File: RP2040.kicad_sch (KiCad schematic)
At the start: 16 parts, among them U1 RP2040

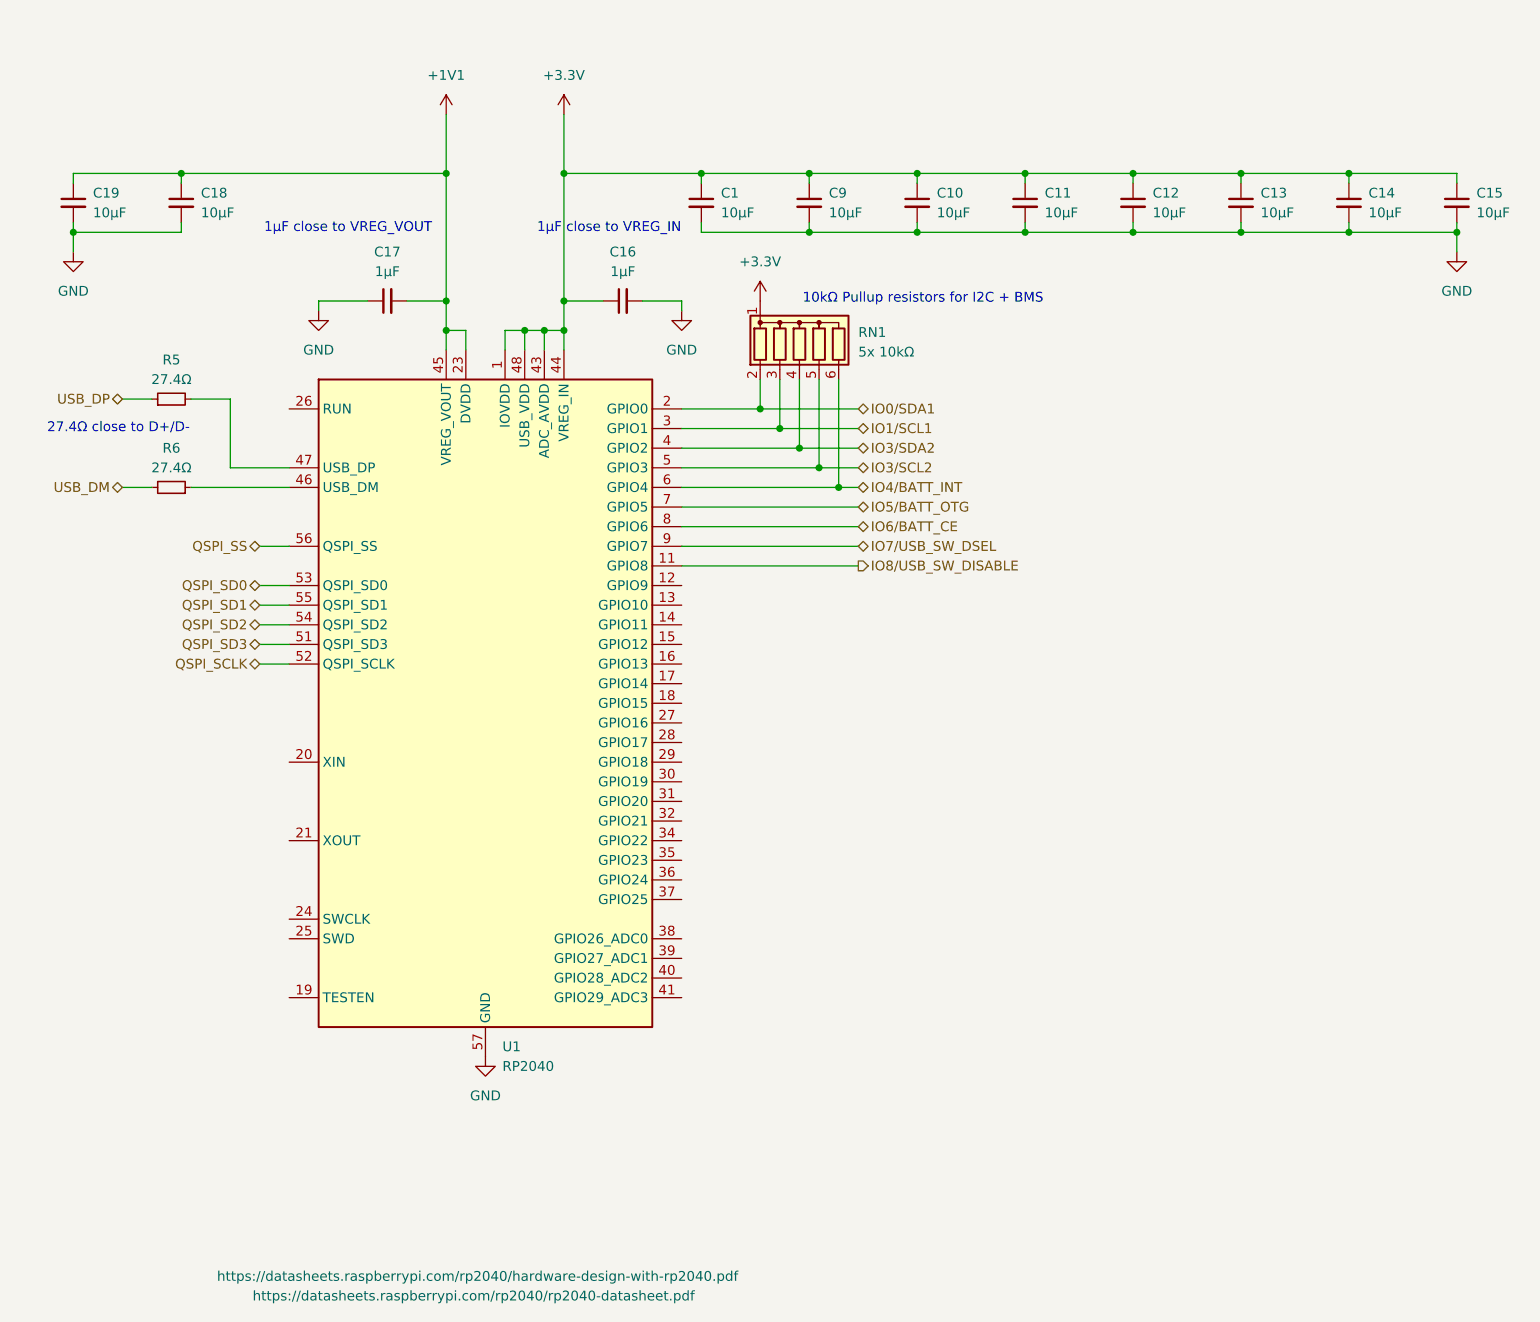
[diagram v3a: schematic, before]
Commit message: BMS updates
Added missing capacitor for OTG
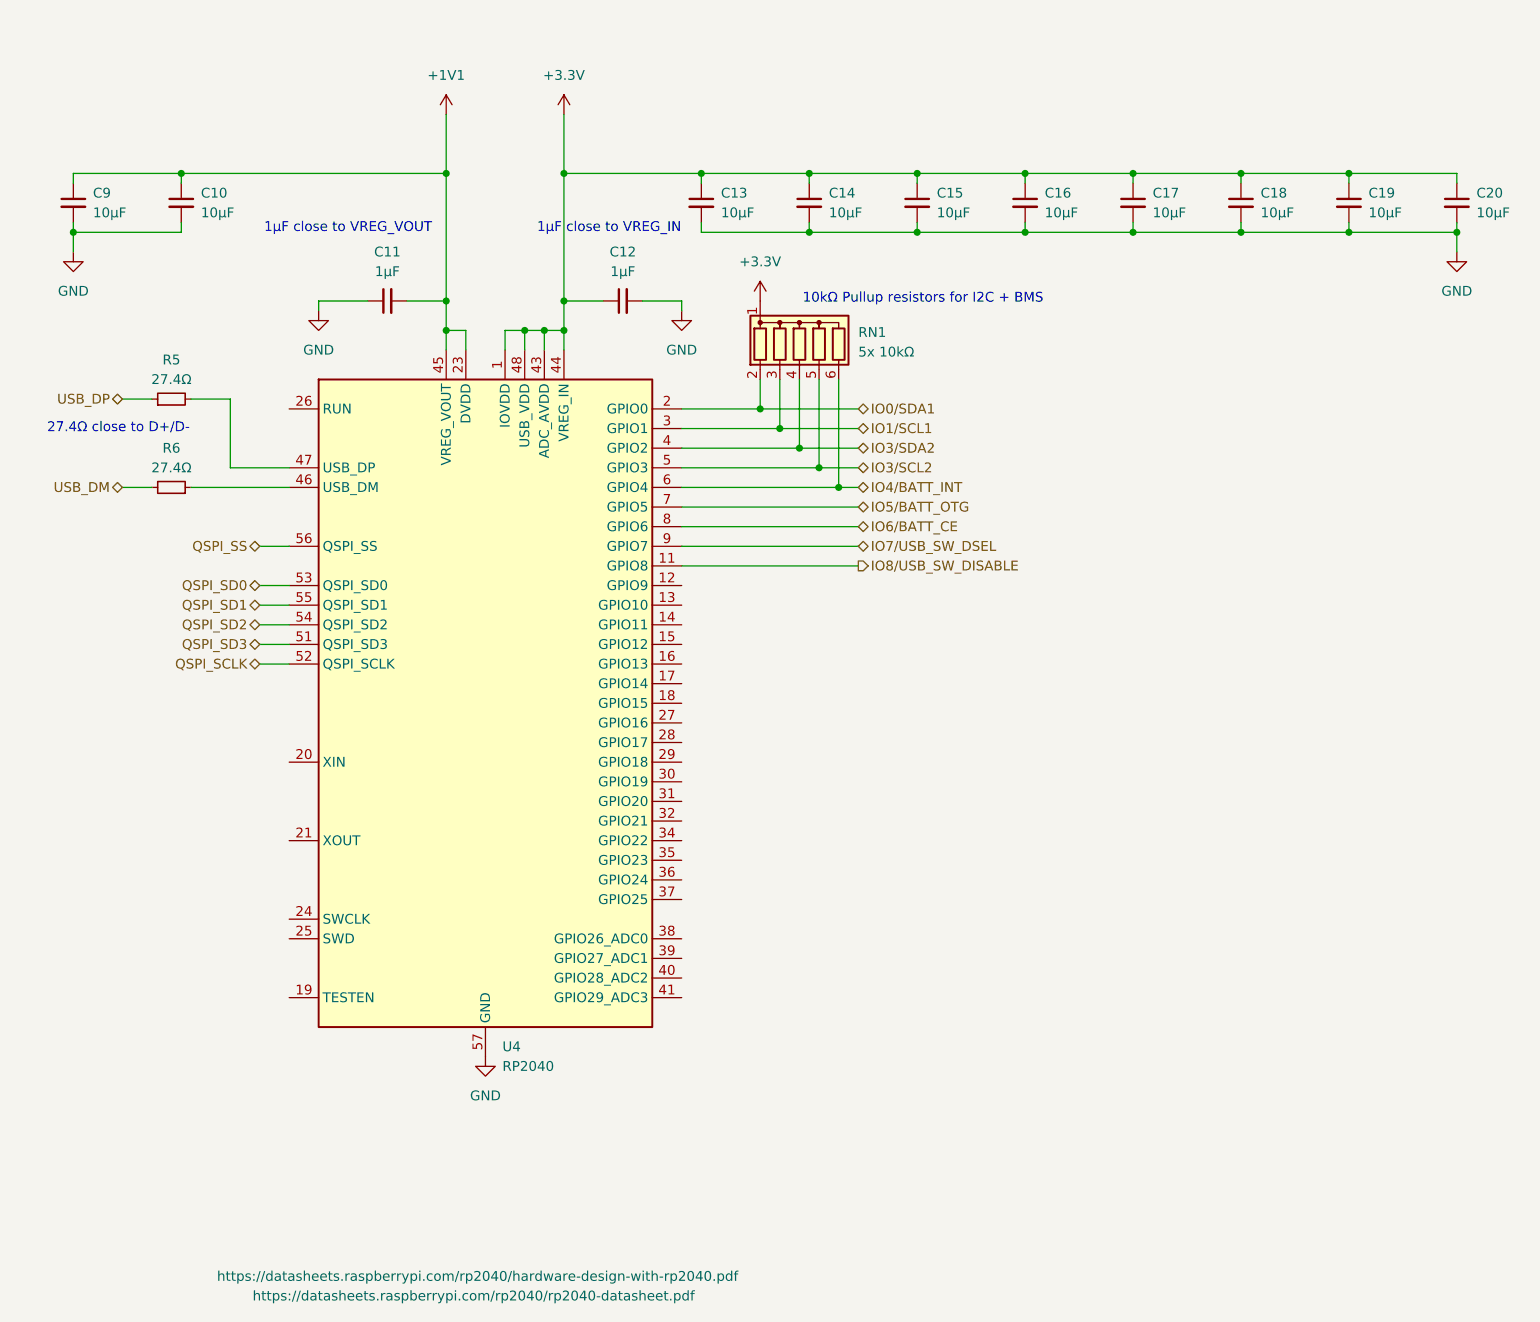
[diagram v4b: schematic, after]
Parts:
- renumbered C18 to C10, C17 to C11, C16 to C12, C1 to C13, C9 to C14, C10 to C15, C11 to C16, C12 to C17, C13 to C18, C14 to C19, C15 to C20, C19 to C9, U1 to U4
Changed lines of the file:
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@@
 		(on_board yes)
 		(dnp no)
-		(property "Reference" "C18"
+		(property "Reference" "C10"
 			(at 69.85 44.45 0)
 			(effects
@@
 			(project "Minibadge Display 5x3"
 				(path "/e5119d15-74fb-4259-abbc-5cab1f368532/9c03ac80-c552-4a59-83c4-4e8b67a63031"
-					(reference "C18")
+					(reference "C10")
 					(unit 1)
 				)
@@
 		(dnp no)
 		(fields_autoplaced yes)
-		(property "Reference" "#PWR01"
+		(property "Reference" "#PWR030"
 			(at 106.68 162.56 0)
 			(effects
@@
 			(project "Minibadge Display 5x3"
 				(path "/e5119d15-74fb-4259-abbc-5cab1f368532/9c03ac80-c552-4a59-83c4-4e8b67a63031"
-					(reference "#PWR01")
+					(reference "#PWR030")
 					(unit 1)
 				)
@@
 		(on_board yes)
 		(dnp no)
-		(property "Reference" "C9"
+		(property "Reference" "C14"
 			(at 151.13 44.45 0)
 			(effects
@@
 			(project ""
 				(path "/e5119d15-74fb-4259-abbc-5cab1f368532/9c03ac80-c552-4a59-83c4-4e8b67a63031"
-					(reference "C9")
+					(reference "C14")
 					(unit 1)
 				)
@@
 		(on_board yes)
 		(dnp no)
-		(property "Reference" "C11"
+		(property "Reference" "C16"
 			(at 179.07 44.45 0)
 			(effects
@@
 			(project "Minibadge Display 5x3"
 				(path "/e5119d15-74fb-4259-abbc-5cab1f368532/9c03ac80-c552-4a59-83c4-4e8b67a63031"
-					(reference "C11")
+					(reference "C16")
 					(unit 1)
 				)
@@
 		(dnp no)
 		(fields_autoplaced yes)
-		(property "Reference" "#PWR0117"
+		(property "Reference" "#PWR029"
 			(at 101.6 38.1 0)
 			(effects
@@
 			(project ""
 				(path "/e5119d15-74fb-4259-abbc-5cab1f368532/9c03ac80-c552-4a59-83c4-4e8b67a63031"
-					(reference "#PWR0117")
+					(reference "#PWR029")
 					(unit 1)
 				)
@@
 		(dnp no)
 		(fields_autoplaced yes)
-		(property "Reference" "#PWR0120"
+		(property "Reference" "#PWR033"
 			(at 142.24 62.23 0)
 			(effects
@@
 			(project ""
 				(path "/e5119d15-74fb-4259-abbc-5cab1f368532/9c03ac80-c552-4a59-83c4-4e8b67a63031"
-					(reference "#PWR0120")
+					(reference "#PWR033")
 					(unit 1)
 				)
@@
 		(on_board yes)
 		(dnp no)
-		(property "Reference" "U1"
+		(property "Reference" "U4"
 			(at 108.8741 154.94 0)
 			(effects
@@
 			(project "Minibadge Display 5x3"
 				(path "/e5119d15-74fb-4259-abbc-5cab1f368532/9c03ac80-c552-4a59-83c4-4e8b67a63031"
-					(reference "U1")
+					(reference "U4")
 					(unit 1)
 				)
@@
 		(on_board yes)
 		(dnp no)
-		(property "Reference" "C1"
+		(property "Reference" "C13"
 			(at 137.16 44.45 0)
 			(effects
@@
 			(project ""
 				(path "/e5119d15-74fb-4259-abbc-5cab1f368532/9c03ac80-c552-4a59-83c4-4e8b67a63031"
-					(reference "C1")
+					(reference "C13")
 					(unit 1)
 				)
@@
 		(dnp no)
 		(fields_autoplaced yes)
-		(property "Reference" "C17"
+		(property "Reference" "C11"
 			(at 93.9863 52.07 90)
 			(effects
@@
 			(project "Minibadge Display 5x3"
 				(path "/e5119d15-74fb-4259-abbc-5cab1f368532/9c03ac80-c552-4a59-83c4-4e8b67a63031"
-					(reference "C17")
+					(reference "C11")
 					(unit 1)
 				)
@@
 		(on_board yes)
 		(dnp no)
-		(property "Reference" "C10"
+		(property "Reference" "C15"
 			(at 165.1 44.45 0)
 			(effects
@@
 			(project "Minibadge Display 5x3"
 				(path "/e5119d15-74fb-4259-abbc-5cab1f368532/9c03ac80-c552-4a59-83c4-4e8b67a63031"
-					(reference "C10")
+					(reference "C15")
 					(unit 1)
 				)
@@
 		(dnp no)
 		(fields_autoplaced yes)
-		(property "Reference" "#PWR0115"
+		(property "Reference" "#PWR034"
 			(at 232.41 58.42 0)
 			(effects
@@
 			(project ""
 				(path "/e5119d15-74fb-4259-abbc-5cab1f368532/9c03ac80-c552-4a59-83c4-4e8b67a63031"
-					(reference "#PWR0115")
+					(reference "#PWR034")
 					(unit 1)
 				)
@@
 		(on_board yes)
 		(dnp no)
-		(property "Reference" "C15"
+		(property "Reference" "C20"
 			(at 234.95 44.45 0)
 			(effects
@@
 			(project "Minibadge Display 5x3"
 				(path "/e5119d15-74fb-4259-abbc-5cab1f368532/9c03ac80-c552-4a59-83c4-4e8b67a63031"
-					(reference "C15")
+					(reference "C20")
 					(unit 1)
 				)
@@
 		(dnp no)
 		(fields_autoplaced yes)
-		(property "Reference" "#PWR0118"
+		(property "Reference" "#PWR032"
 			(at 132.08 66.04 0)
 			(effects
@@
 			(project "Minibadge Display 5x3"
 				(path "/e5119d15-74fb-4259-abbc-5cab1f368532/9c03ac80-c552-4a59-83c4-4e8b67a63031"
-					(reference "#PWR0118")
+					(reference "#PWR032")
 					(unit 1)
 				)
@@
 		(on_board yes)
 		(dnp no)
-		(property "Reference" "C19"
+		(property "Reference" "C9"
 			(at 55.88 44.45 0)
 			(effects
@@
 			(project "Minibadge Display 5x3"
 				(path "/e5119d15-74fb-4259-abbc-5cab1f368532/9c03ac80-c552-4a59-83c4-4e8b67a63031"
-					(reference "C19")
+					(reference "C9")
 					(unit 1)
 				)
@@
 		(on_board yes)
 		(dnp no)
-		(property "Reference" "C14"
+		(property "Reference" "C19"
 			(at 220.98 44.45 0)
 			(effects
@@
 			(project "Minibadge Display 5x3"
 				(path "/e5119d15-74fb-4259-abbc-5cab1f368532/9c03ac80-c552-4a59-83c4-4e8b67a63031"
-					(reference "C14")
+					(reference "C19")
 					(unit 1)
 				)
@@
 		(dnp no)
 		(fields_autoplaced yes)
-		(property "Reference" "#PWR0116"
+		(property "Reference" "#PWR028"
 			(at 85.09 66.04 0)
 			(effects
@@
 			(project "Minibadge Display 5x3"
 				(path "/e5119d15-74fb-4259-abbc-5cab1f368532/9c03ac80-c552-4a59-83c4-4e8b67a63031"
-					(reference "#PWR0116")
+					(reference "#PWR028")
 					(unit 1)
 				)
@@
 		(on_board yes)
 		(dnp no)
-		(property "Reference" "C13"
+		(property "Reference" "C18"
 			(at 207.01 44.45 0)
 			(effects
@@
 			(project "Minibadge Display 5x3"
 				(path "/e5119d15-74fb-4259-abbc-5cab1f368532/9c03ac80-c552-4a59-83c4-4e8b67a63031"
-					(reference "C13")
+					(reference "C18")
 					(unit 1)
 				)
@@
 		(dnp no)
 		(fields_autoplaced yes)
-		(property "Reference" "C16"
+		(property "Reference" "C12"
 			(at 124.4663 52.07 90)
 			(effects
@@
 			(project ""
 				(path "/e5119d15-74fb-4259-abbc-5cab1f368532/9c03ac80-c552-4a59-83c4-4e8b67a63031"
-					(reference "C16")
+					(reference "C12")
 					(unit 1)
 				)
@@
 		(dnp no)
 		(fields_autoplaced yes)
-		(property "Reference" "#PWR0119"
+		(property "Reference" "#PWR027"
 			(at 53.34 58.42 0)
 			(effects
@@
 			(project ""
 				(path "/e5119d15-74fb-4259-abbc-5cab1f368532/9c03ac80-c552-4a59-83c4-4e8b67a63031"
-					(reference "#PWR0119")
+					(reference "#PWR027")
 					(unit 1)
 				)
@@
 		(dnp no)
 		(fields_autoplaced yes)
-		(property "Reference" "#PWR0121"
+		(property "Reference" "#PWR031"
 			(at 116.84 38.1 0)
 			(effects
@@
 			(project ""
 				(path "/e5119d15-74fb-4259-abbc-5cab1f368532/9c03ac80-c552-4a59-83c4-4e8b67a63031"
-					(reference "#PWR0121")
+					(reference "#PWR031")
 					(unit 1)
 				)
@@
 		(on_board yes)
 		(dnp no)
-		(property "Reference" "C12"
+		(property "Reference" "C17"
 			(at 193.04 44.45 0)
 			(effects
@@
 			(project "Minibadge Display 5x3"
 				(path "/e5119d15-74fb-4259-abbc-5cab1f368532/9c03ac80-c552-4a59-83c4-4e8b67a63031"
-					(reference "C12")
-					(unit 1)
-				)
+					(reference "C17")
+					(unit 1)
+				)
